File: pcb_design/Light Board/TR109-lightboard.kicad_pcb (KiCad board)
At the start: 2 copper layers, 49.7 x 18.2 mm, 14 parts, among them J1 Conn_01x05_Female

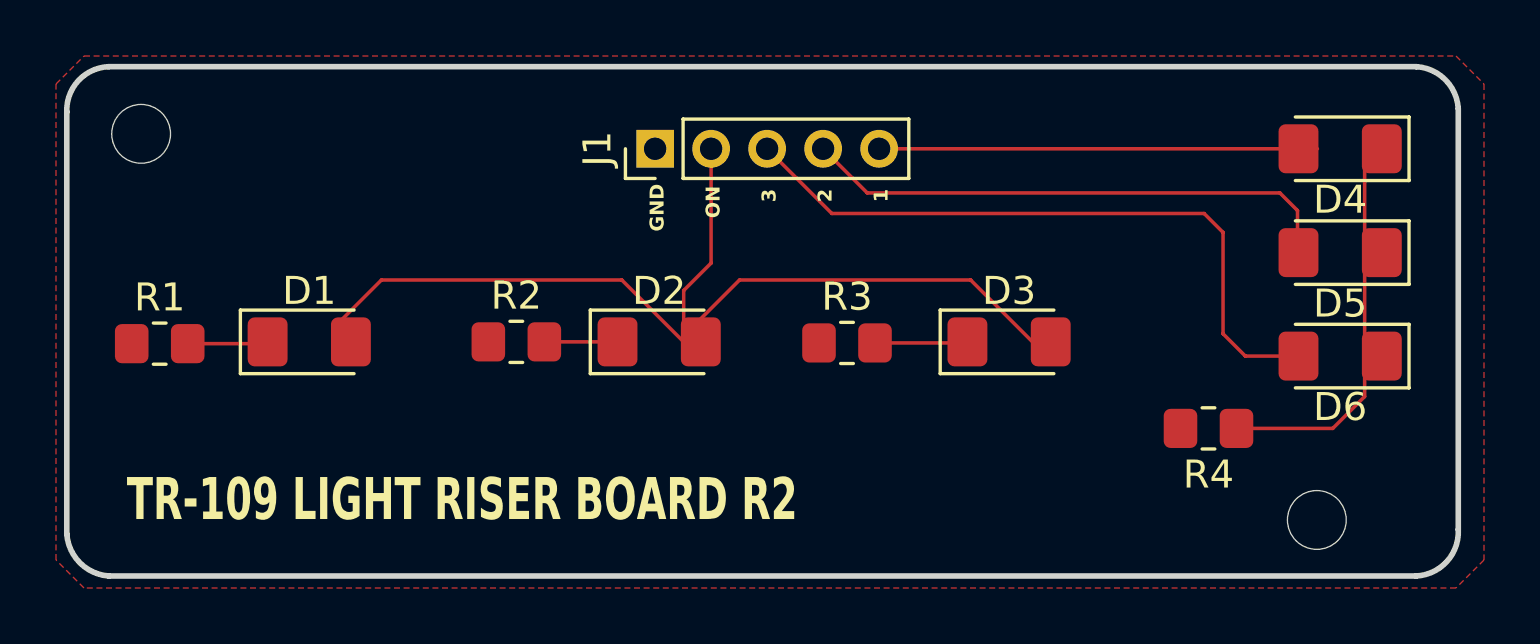
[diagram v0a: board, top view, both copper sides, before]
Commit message: Fixed some kicad PCB errors, updated Blender file
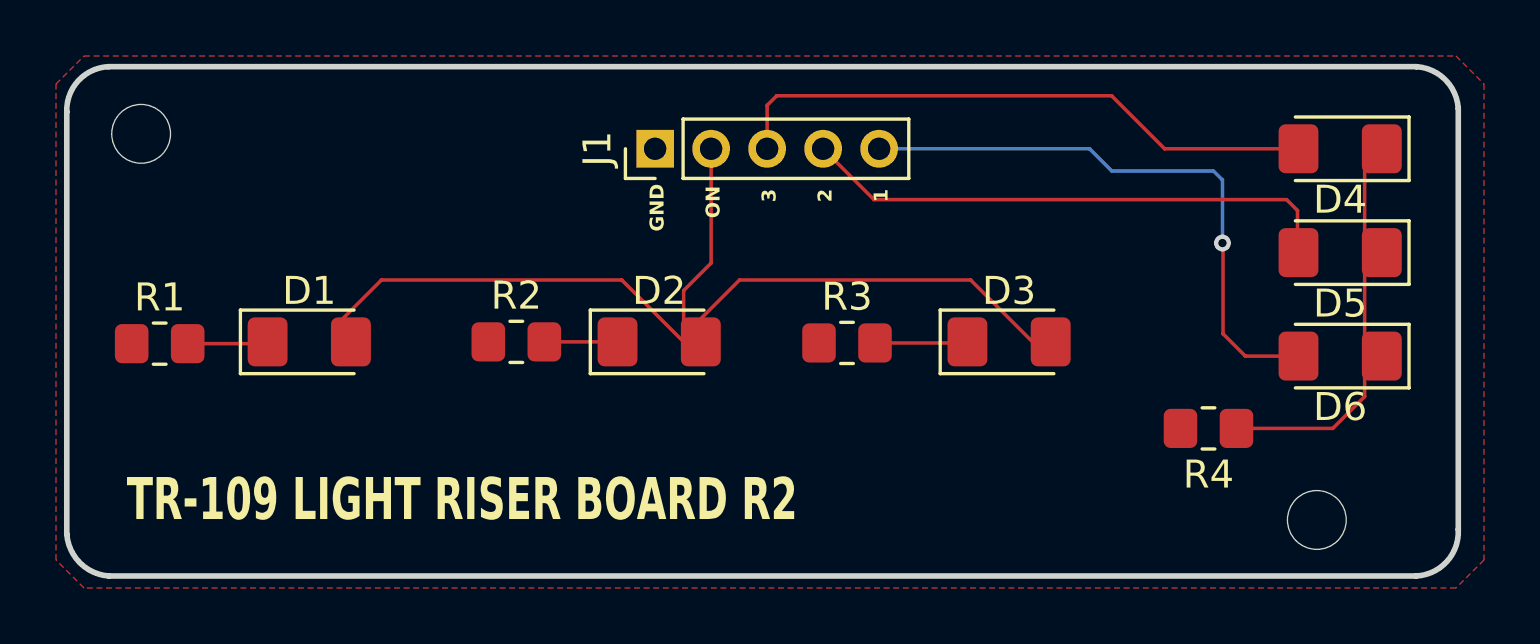
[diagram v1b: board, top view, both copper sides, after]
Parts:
- D1, D2, D3: value Yellow_LED -> LED
- D4: value Red_LED -> LED
- D5, D6: value Green_LED -> LED
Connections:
- J1 pad 3: L3 -> L1
- J1 pad 5: L1 -> L3
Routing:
- net L1: track 15.7 -> 21.5 mm
- net L3: track 24.2 -> 21.2 mm, vias 0 -> 1
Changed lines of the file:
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@@
 			)
 		)
-		(property "Value" "Yellow_LED"
+		(property "Value" "LED"
 			(at 0 1.82 0)
 			(layer "F.Fab")
@@
 			)
 		)
-		(property "Value" "Yellow_LED"
+		(property "Value" "LED"
 			(at 0 1.82 0)
 			(layer "F.Fab")
@@
 			)
 		)
-		(property "Value" "Yellow_LED"
+		(property "Value" "LED"
 			(at 0 1.82 0)
 			(layer "F.Fab")
@@
 			)
 		)
-		(property "Value" "Red_LED"
+		(property "Value" "LED"
 			(at 0 1.82 0)
 			(layer "F.Fab")
@@
 			)
 		)
-		(property "Value" "Green_LED"
+		(property "Value" "LED"
 			(at 0 1.82 0)
 			(layer "F.Fab")
@@
 			)
 		)
-		(property "Value" "Green_LED"
+		(property "Value" "LED"
 			(at 0 1.82 0)
 			(layer "F.Fab")
@@
 			(layers "*.Cu" "*.Mask")
 			(remove_unused_layers no)
-			(net 4 "L3")
+			(net 2 "L1")
 			(pinfunction "Pin_3")
 			(pintype "passive")
@@
 			(layers "*.Cu" "*.Mask")
 			(remove_unused_layers no)
-			(net 2 "L1")
+			(net 4 "L3")
 			(pinfunction "Pin_5")
 			(pintype "passive")
@@
 	)
 	(segment
-		(start 153.396704 95.3135)
-		(end 169.051 95.3135)
+		(start 168.375 95.3135)
+		(end 163.5935 95.3135)
 		(width 0.127)
 		(layer "F.Cu")
@@
 	)
 	(segment
-		(start 167.71 96.89)
-		(end 168.34 97.52)
+		(start 149.396704 93.763296)
+		(end 149.396704 95.3135)
 		(width 0.127)
 		(layer "F.Cu")
-		(net 3)
+		(net 2)
 	)
 	(segment
-		(start 152.973204 96.89)
-		(end 167.71 96.89)
+		(start 161.7 93.42)
+		(end 149.74 93.42)
+		(width 0.127)
+		(layer "F.Cu")
+		(net 2)
+	)
+	(segment
+		(start 163.5935 95.3135)
+		(end 161.7 93.42)
+		(width 0.127)
+		(layer "F.Cu")
+		(net 2)
+	)
+	(segment
+		(start 149.74 93.42)
+		(end 149.396704 93.763296)
+		(width 0.127)
+		(layer "F.Cu")
+		(net 2)
+	)
+	(segment
+		(start 153.213204 97.13)
+		(end 167.95 97.13)
 		(width 0.127)
 		(layer "F.Cu")
@@
 	(segment
 		(start 151.396704 95.3135)
-		(end 152.973204 96.89)
+		(end 153.213204 97.13)
 		(width 0.127)
 		(layer "F.Cu")
@@
 	)
 	(segment
-		(start 165.68 98.3)
-		(end 165.68 101.92)
+		(start 167.95 97.13)
+		(end 168.34 97.52)
+		(width 0.127)
+		(layer "F.Cu")
+		(net 3)
+	)
+	(segment
+		(start 165.68 101.92)
+		(end 165.68 98.7)
 		(width 0.127)
 		(layer "F.Cu")
@@
 	)
 	(segment
-		(start 149.396704 95.3135)
-		(end 151.708104 97.6249)
+		(start 165.68 98.7)
+		(end 165.66 98.68)
 		(width 0.127)
 		(layer "F.Cu")
 		(net 4)
 	)
+	(via
+		(at 165.66 98.68)
+		(size 0.6)
+		(drill 0.3)
+		(layers "F.Cu" "B.Cu")
+		(net 4)
+	)
 	(segment
-		(start 151.708104 97.6249)
-		(end 165.0049 97.6249)
+		(start 160.9135 95.3135)
+		(end 153.396704 95.3135)
 		(width 0.127)
-		(layer "F.Cu")
+		(layer "B.Cu")
 		(net 4)
 	)
 	(segment
-		(start 165.0049 97.6249)
-		(end 165.68 98.3)
+		(start 165.34 96.11)
+		(end 161.71 96.11)
 		(width 0.127)
-		(layer "F.Cu")
+		(layer "B.Cu")
+		(net 4)
+	)
+	(segment
+		(start 165.66 96.43)
+		(end 165.34 96.11)
+		(width 0.127)
+		(layer "B.Cu")
+		(net 4)
+	)
+	(segment
+		(start 165.66 98.68)
+		(end 165.66 96.43)
+		(width 0.127)
+		(layer "B.Cu")
+		(net 4)
+	)
+	(segment
+		(start 161.71 96.11)
+		(end 160.9135 95.3135)
+		(width 0.127)
+		(layer "B.Cu")
 		(net 4)
 	)
